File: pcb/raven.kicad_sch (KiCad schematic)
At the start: 45 parts, among them J1 Conn_02x20_Odd_Even, J2 Conn_01x04_MountingPin, J3 Conn_01x02_Pin, J4 Conn_01x02_Pin, J5 Conn_01x04_MountingPin, J6 Conn_01x02_Pin, J7 Conn_01x02_Pin, J8 Conn_01x02_Pin, J9 Conn_01x02_Pin, U9 TPS548B28RWWR

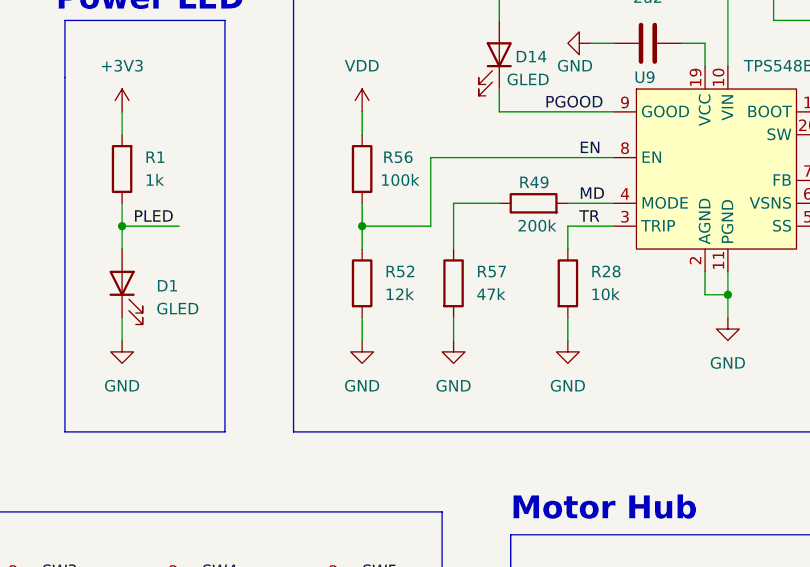
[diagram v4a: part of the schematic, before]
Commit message: Change cutoff voltage
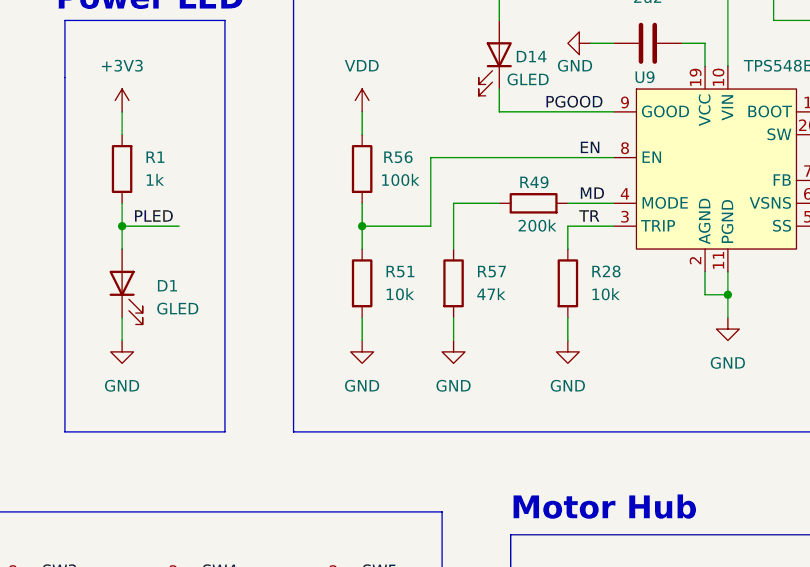
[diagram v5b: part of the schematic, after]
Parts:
- removed R52: 12k, Resistor_SMD:R_0402_1005Metric, symbol Device:R
- added R51: 10k, Resistor_SMD:R_0402_1005Metric, symbol Device:R
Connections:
- net EN: now also R51.1
- net GND: now also R51.2
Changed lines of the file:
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@@
-	)
-	(symbol
-		(lib_id "Device:R")
-		(at 104.14 143.51 0)
-		(unit 1)
-		(exclude_from_sim no)
-		(in_bom yes)
-		(on_board yes)
-		(dnp no)
-		(fields_autoplaced yes)
-		(property "Reference" "R52"
-			(at 106.68 142.2399 0)
-			(effects
-				(font
-					(size 1.27 1.27)
-				)
-				(justify left)
-			)
-		)
-		(property "Value" "12k"
-			(at 106.68 144.7799 0)
-			(effects
-				(font
-					(size 1.27 1.27)
-				)
-				(justify left)
-			)
-		)
-		(property "Footprint" "Resistor_SMD:R_0402_1005Metric"
-			(at 102.362 143.51 90)
-			(effects
-				(font
-					(size 1.27 1.27)
-				)
-				(hide yes)
-			)
-		)
-		(property "Datasheet" "~"
-			(at 104.14 143.51 0)
-			(effects
-				(font
-					(size 1.27 1.27)
-				)
-				(hide yes)
-			)
-		)
-		(property "Description" "Resistor"
-			(at 104.14 143.51 0)
-			(effects
-				(font
-					(size 1.27 1.27)
-				)
-				(hide yes)
-			)
-		)
-		(property "LCSC" "C25752"
-			(at 104.14 143.51 0)
-			(effects
-				(font
-					(size 1.27 1.27)
-				)
-				(hide yes)
-			)
-		)
-		(pin "1"
-		)
-		(pin "2"
-		)
-		(instances
-			(project "raven"
-				(path "/38b0a34b-2047-47f6-90d7-ccdf77e8e212"
-					(reference "R52")
-					(unit 1)
-				)
-			)
-		)
 	)
 	(symbol
@@
 					(unit 1)
 				)
+			)
+		)
+	)
+	(symbol
+		(lib_id "Device:R")
+		(at 104.14 143.51 0)
+		(unit 1)
+		(exclude_from_sim no)
+		(in_bom yes)
+		(on_board yes)
+		(dnp no)
+		(fields_autoplaced yes)
+		(property "Reference" "R51"
+			(at 106.68 142.2399 0)
+			(effects
+				(font
+					(size 1.27 1.27)
+				)
+				(justify left)
+			)
+		)
+		(property "Value" "10k"
+			(at 106.68 144.7799 0)
+			(effects
+				(font
+					(size 1.27 1.27)
+				)
+				(justify left)
+			)
+		)
+		(property "Footprint" "Resistor_SMD:R_0402_1005Metric"
+			(at 102.362 143.51 90)
+			(effects
+				(font
+					(size 1.27 1.27)
+				)
+				(hide yes)
+			)
+		)
+		(property "Datasheet" "~"
+			(at 104.14 143.51 0)
+			(effects
+				(font
+					(size 1.27 1.27)
+				)
+				(hide yes)
+			)
+		)
+		(property "Description" "Resistor"
+			(at 104.14 143.51 0)
+			(effects
+				(font
+					(size 1.27 1.27)
+				)
+				(hide yes)
+			)
+		)
+		(property "LCSC" "C25744"
+			(at 104.14 143.51 0)
+			(effects
+				(font
+					(size 1.27 1.27)
+				)
+				(hide yes)
+			)
+		)
+		(pin "1"
+		)
+		(pin "2"
+		)
+		(instances
+			(project "raven"
+				(path "/38b0a34b-2047-47f6-90d7-ccdf77e8e212"
+					(reference "R51")
+					(unit 1)
+				)

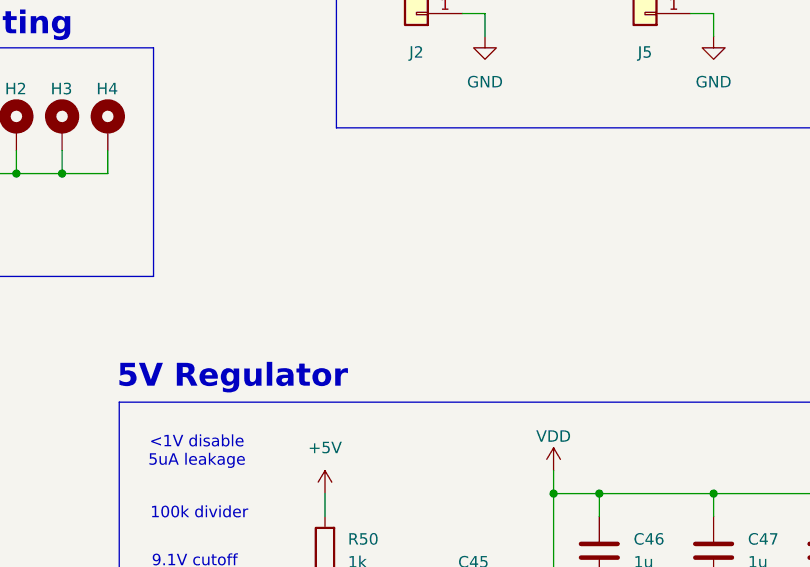
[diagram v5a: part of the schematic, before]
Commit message: Plan adding power switch
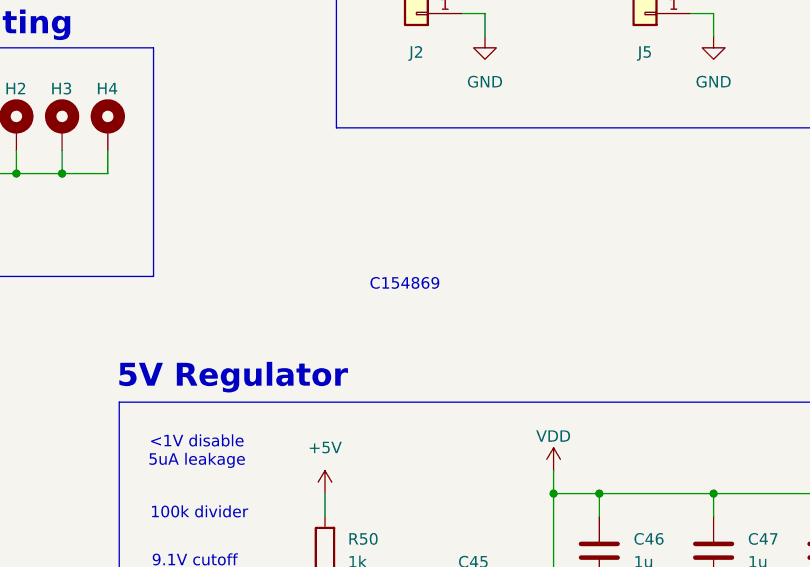
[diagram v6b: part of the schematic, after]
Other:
- note added: "C154869"
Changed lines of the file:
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@@
+		)
+	)
+	(text "C154869"
+		(exclude_from_sim no)
+		(at 128.27 78.486 0)
+		(effects
+			(font
+				(size 1.27 1.27)
+			)
 		)
 	)

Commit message: Add power switch
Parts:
- added J11: Conn_01x02_Pin, Connector_JST:JST_PH_B2B-PH-K_1x02_P2.00mm_Vertical, symbol Connector:Conn_01x02_Pin
- added Q1: DMP2002UPS, Footprints:DMP2002UPS, symbol Symbols:DMP2002UPS
- added R52, R58: 10k, Resistor_SMD:R_0402_1005Metric, symbol Device:R
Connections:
- net GND: now also J11.2 (Pin_2)
- net VDD: now also Q1.1 (S), Q1.2 (S), Q1.3 (S), R52.2; no longer F1.1
- net VDDF: no longer names the net of F1.2, J3.2 (Pin_2)
- new net: Q1.4 (G), R52.1, R58.1
- new net: F1.1, Q1.5 (D), Q1.6 (D), Q1.7 (D), Q1.8 (D)
- new net: J11.1 (Pin_1), R58.2
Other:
- note removed: "C154869"
- moved on the sheet: C1, C23, C39, C40, C41, C42, C43, C44, C45, C46, C47, C48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

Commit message: Finish for revision 2 production
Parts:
- removed C1: 100u, Capacitor_SMD:C_Elec_8x6.2, symbol Device:C
- removed Q1: DMP2002UPS, Footprints:DMP2002UPS, symbol Symbols:DMP2002UPS
- added C28: 10u, Capacitor_SMD:C_0603_1608Metric, symbol Device:C
- added Q1: AO3400A, Package_TO_SOT_SMD:SOT-23, symbol Transistor_FET:AO3400A
- added Q3: DMP2002UPS, Footprints:DMP2002UPS, symbol Symbols:DMP2002UPS
- added R66: 7k5, Resistor_SMD:R_0402_1005Metric, symbol Device:R
- J1, J11, J3, J4, J6, J7, J8, J9: now not fitted
- L1: value 330nH -> 1u; footprint Inductor_SMD:L_Changjiang_FXL0630 -> Footprints:L_0660A; LCSC C167211 -> C18199443
- R28, R51, R52, R54: value 10k -> 7k5; LCSC C25744 -> C25918
- R49: value 200k -> 7k5; LCSC C25764 -> C25918
- R53: value 75k -> 56k; LCSC C25798 -> C25796
- R56: value 100k -> 47k; LCSC C25741 -> C25792
- R57: value 47k -> 56k; LCSC C25792 -> C25796
- R58: value 10k -> 100k; LCSC C25744 -> C25741
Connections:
- net GND: now also D14.1 (K), R49.2, Q1.2 (S)
- net MD: now also R57.1; no longer R49.2
- net PGOOD: now also D14.2 (A), R50.1; no longer D14.1 (K)
- net VDD: now also Q3.5 (D), Q3.6 (D), Q3.7 (D), Q3.8 (D); no longer R52.2
- net at R58.1: now also J11.1 (Pin_1), C28.1; no longer R52.1
- net at F1.1: now also J3.2 (Pin_2)
- net at F1.2: now also Q3.1 (S), Q3.2 (S), Q3.3 (S), R66.1; no longer J3.2 (Pin_2)
- net at R58.2: now also R52.2, C28.2, Q1.3 (D); no longer J11.1 (Pin_1)
- net PWR: now reaches R49.1
- net PWR: now also Q1.1 (G); no longer R57.1
- new net: Q3.4 (G), R52.1, R66.2
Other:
- sheet MotorHub ports: added PWR; removed none
- note added: "Continuous Condution Mode for better ripple"
- note added: "I_out = 16A"
- note added: "V_out = 5.08V"
- note added: "f_sw = 975kHz"
- note removed: "100k divider"
- note removed: "9.1V cutoff"
- note removed: "<1V disable 5uA leakage"
- note removed: "Bulk Cap"
- note removed: "Discontinuous Condution Mode (skip-mode) for better effeciency"
- note removed: "I_out = 12A (peak = 14A)"
- note removed: "V_out = 5.1V"
- note removed: "f_sw = 800khz"
- moved on the sheet: C23, C39, C40, C41, C42, C43, C44, C45, C46, C47, C48, C49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
